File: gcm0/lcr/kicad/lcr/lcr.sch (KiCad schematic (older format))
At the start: 55 parts

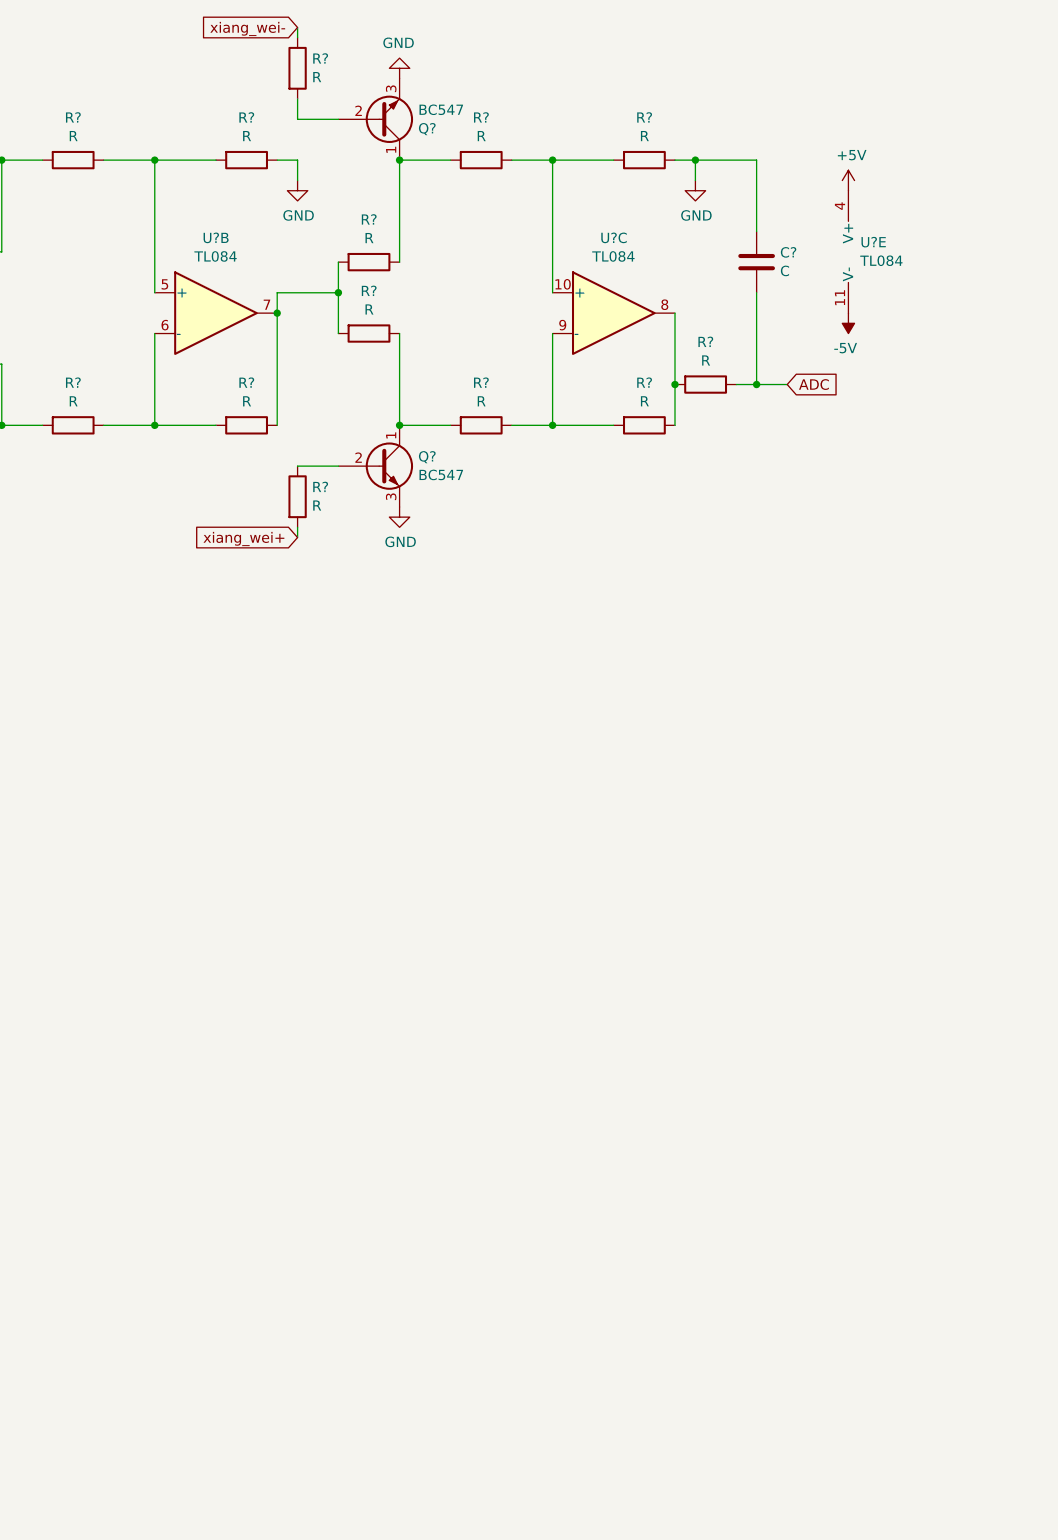
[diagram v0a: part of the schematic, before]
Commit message: 显示实部虚部
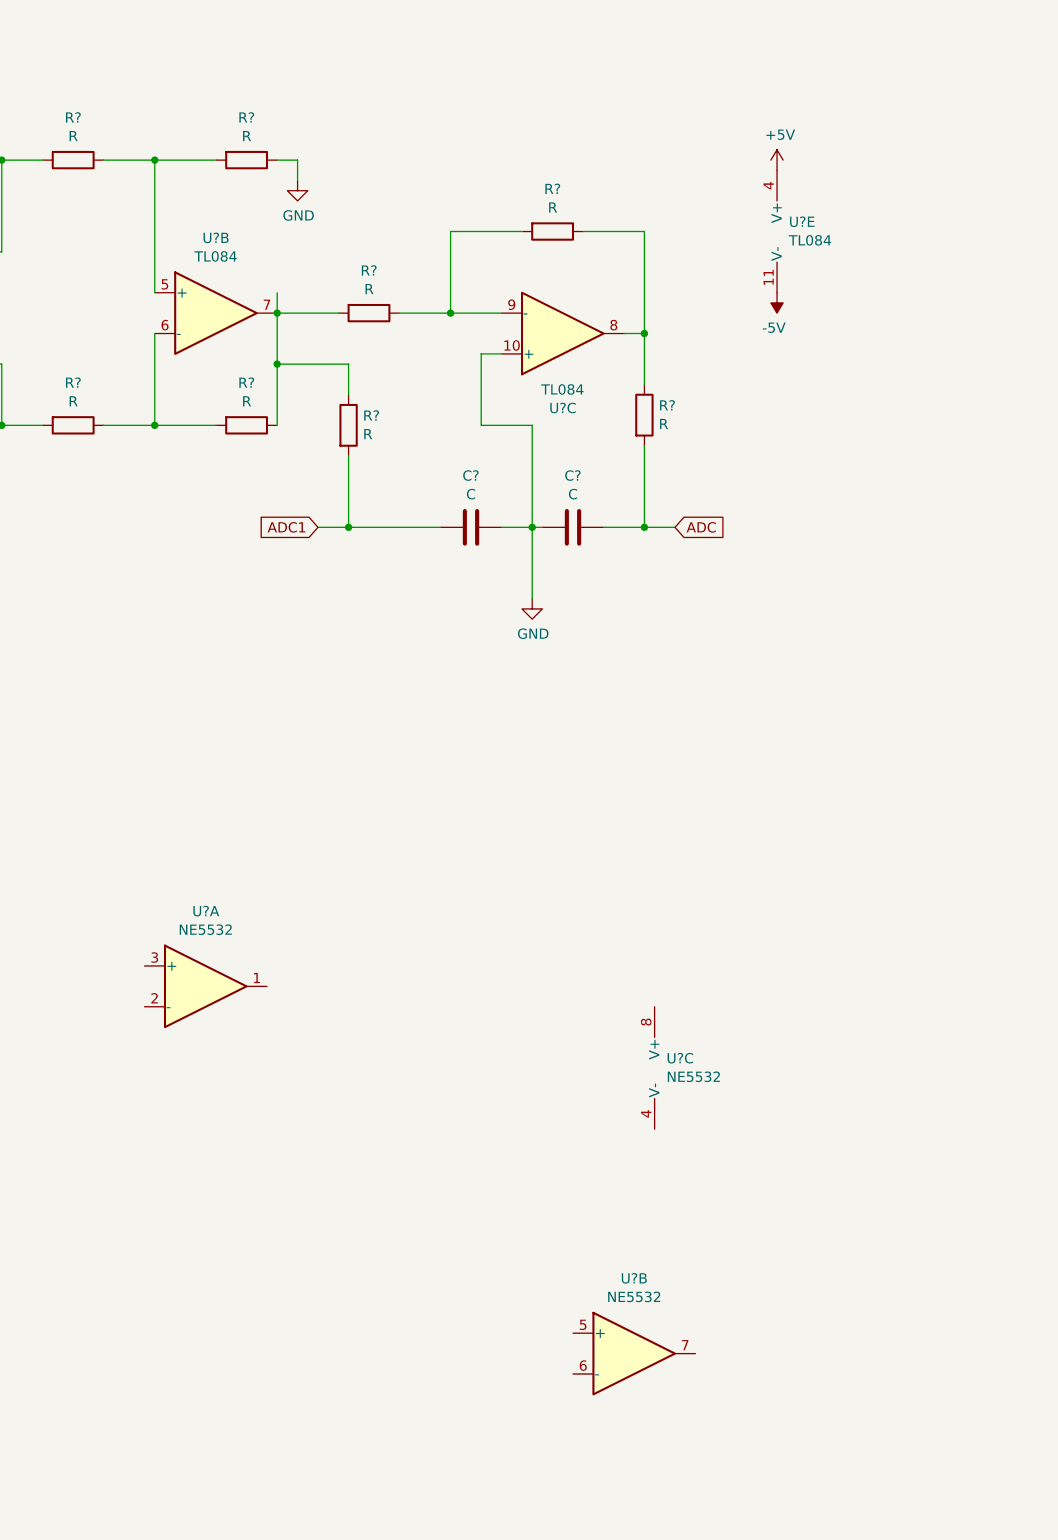
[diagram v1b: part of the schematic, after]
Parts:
- removed C?: C, symbol Device:C
- removed Q? (x2): BC547, Package_TO_SOT_THT:TO-92_Inline, symbol Transistor_BJT:BC547
- removed R? (x9): R, symbol Device:R
- added C? (x2): C, symbol Device:C
- added R? (x4): R, symbol Device:R
- added U? (x3): NE5532, symbol Amplifier_Operational:NE5532
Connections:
- net ADC: now also C?.1, R?.2
- net GND: now also U?.10 (+), C?.1, C?.2
- net at R?.1, U?.7: now also R?.1, R?.2
- net at U?.8: now also R?.1, R?.1
- net at U?.9 (-): now also R?.1, R?.2
- new net ADC1: C?.2, R?.2
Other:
- moved on the sheet: U?C, U?E
